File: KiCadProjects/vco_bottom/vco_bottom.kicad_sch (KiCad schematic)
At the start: 93 parts, among them J1 Conn_02x08_Odd_Even, J2 Conn_02x08_Odd_Even, J3 Conn_01x03_Pin, J4 Conn_01x03_Pin, J5 Conn_01x03_Pin, J6 Conn_02x08_Odd_Even, Q1 BC558, Q2 BC548, Q3 BC558, Q4 BC548, Q5 BC558, Q6 BC548, U1 40106, U2 TL074, U3 TL074, U4 TL074

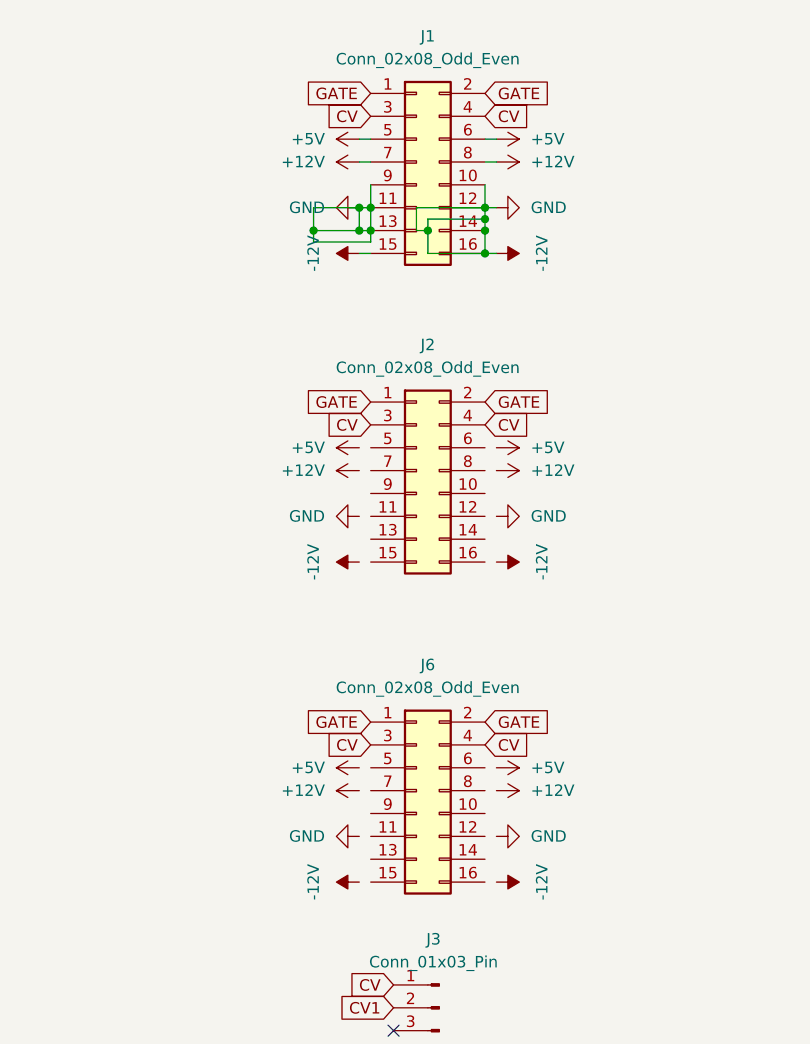
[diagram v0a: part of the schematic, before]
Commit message: added vco top and bottom
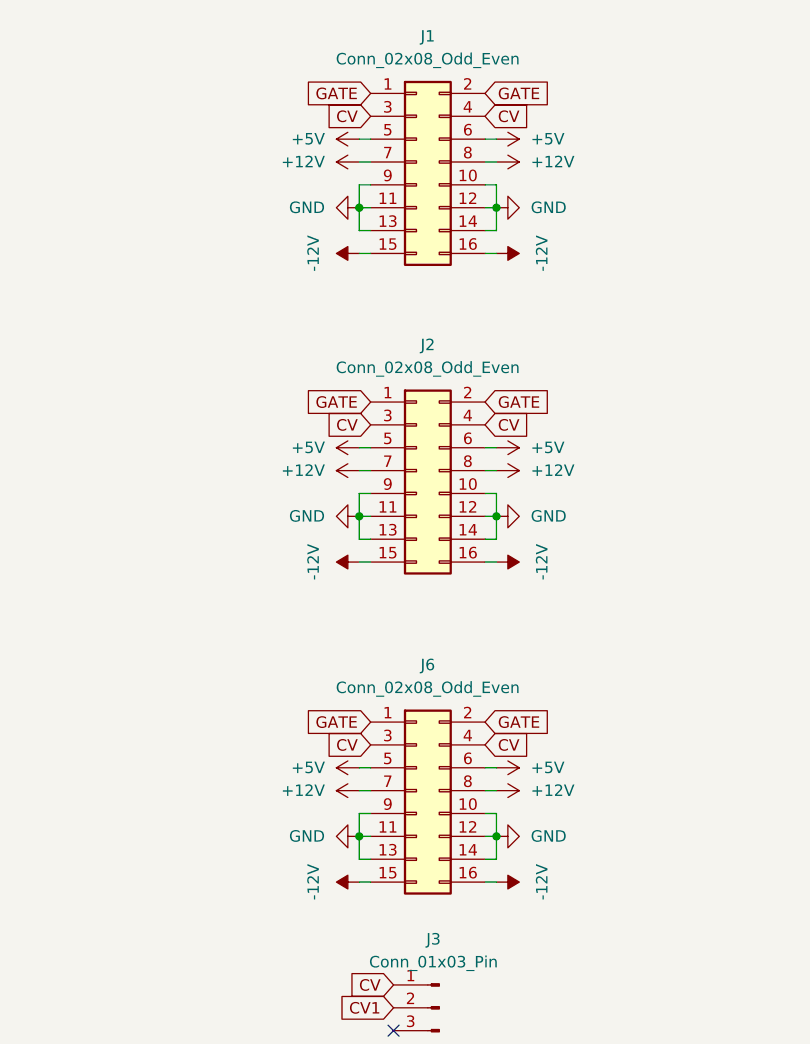
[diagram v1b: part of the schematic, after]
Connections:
- net +12V: now also J2.7 (Pin_7), J2.8 (Pin_8), J6.7 (Pin_7), J6.8 (Pin_8)
- net +5V: now also J2.5 (Pin_5), J2.6 (Pin_6), J6.5 (Pin_5), J6.6 (Pin_6)
- net -12V: now also J2.15 (Pin_15), J2.16 (Pin_16), J6.15 (Pin_15), J6.16 (Pin_16); no longer C1.2, C10.2, C11.1, C12.2, C13.1, C14.2, C15.1, C16.2, C4.2, C7.2, J1.10 (Pin_10), J1.11 (Pin_11), J1.12 (Pin_12), J1.13 (Pin_13), J1.14 (Pin_14), J1.9 (Pin_9), Q2.3 (E), Q4.3 (E), Q6.3 (E), R12.2, R14.2, R20.2, R22.2, R23.2, R26.2, R28.2, R34.2, R36.2, R37.2, R40.2, R42.2, R6.2, R8.2, R9.2, T1.0 (Pin_0), T1.15 (Pin_15), T1.17 (Pin_17), T1.2 (Pin_2), T1.30 (Pin_30), U1.7 (VSS)
- net GND: now reaches J6.10 (Pin_10)
- net GND: now also C1.2, C10.2, C11.1, C12.2, C13.1, C14.2, C15.1, C16.2, C4.2, C7.2, J1.10 (Pin_10), J1.11 (Pin_11), J1.12 (Pin_12), J1.13 (Pin_13), J1.14 (Pin_14), J1.9 (Pin_9), J2.10 (Pin_10), J2.11 (Pin_11), J2.12 (Pin_12), J2.13 (Pin_13), J2.14 (Pin_14), J2.9 (Pin_9), J6.11 (Pin_11), J6.12 (Pin_12), J6.13 (Pin_13), J6.14 (Pin_14), J6.9 (Pin_9), Q2.3 (E), Q4.3 (E), Q6.3 (E), R12.2, R14.2, R20.2, R22.2, R23.2, R26.2, R28.2, R34.2, R36.2, R37.2, R40.2, R42.2, R6.2, R8.2, R9.2, T1.0 (Pin_0), T1.15 (Pin_15), T1.17 (Pin_17), T1.2 (Pin_2), T1.30 (Pin_30), U1.7 (VSS)
